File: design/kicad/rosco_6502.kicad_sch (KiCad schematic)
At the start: 58 parts, among them IC1 W65C02SxP, IC2 ATF22V10C-7PX, IC3 XR68C681CJTR-F, IC4 NE555P, IC5 ATF22V10C-7PX, J1 UART_A, J2 UART_B, J3 Conn_01x06, J4 Conn_01x01_Male, J5 Conn_02x18_Odd_Even, J6 Conn_01x02_Pin, J7 Jack-DC, Q1 3.6864MHz, U1 AS6C4008-55PCN, U2 AS6C62256-55PCN, U3 AT28C256-15PU, U4 74HCT174, X1 14MHz

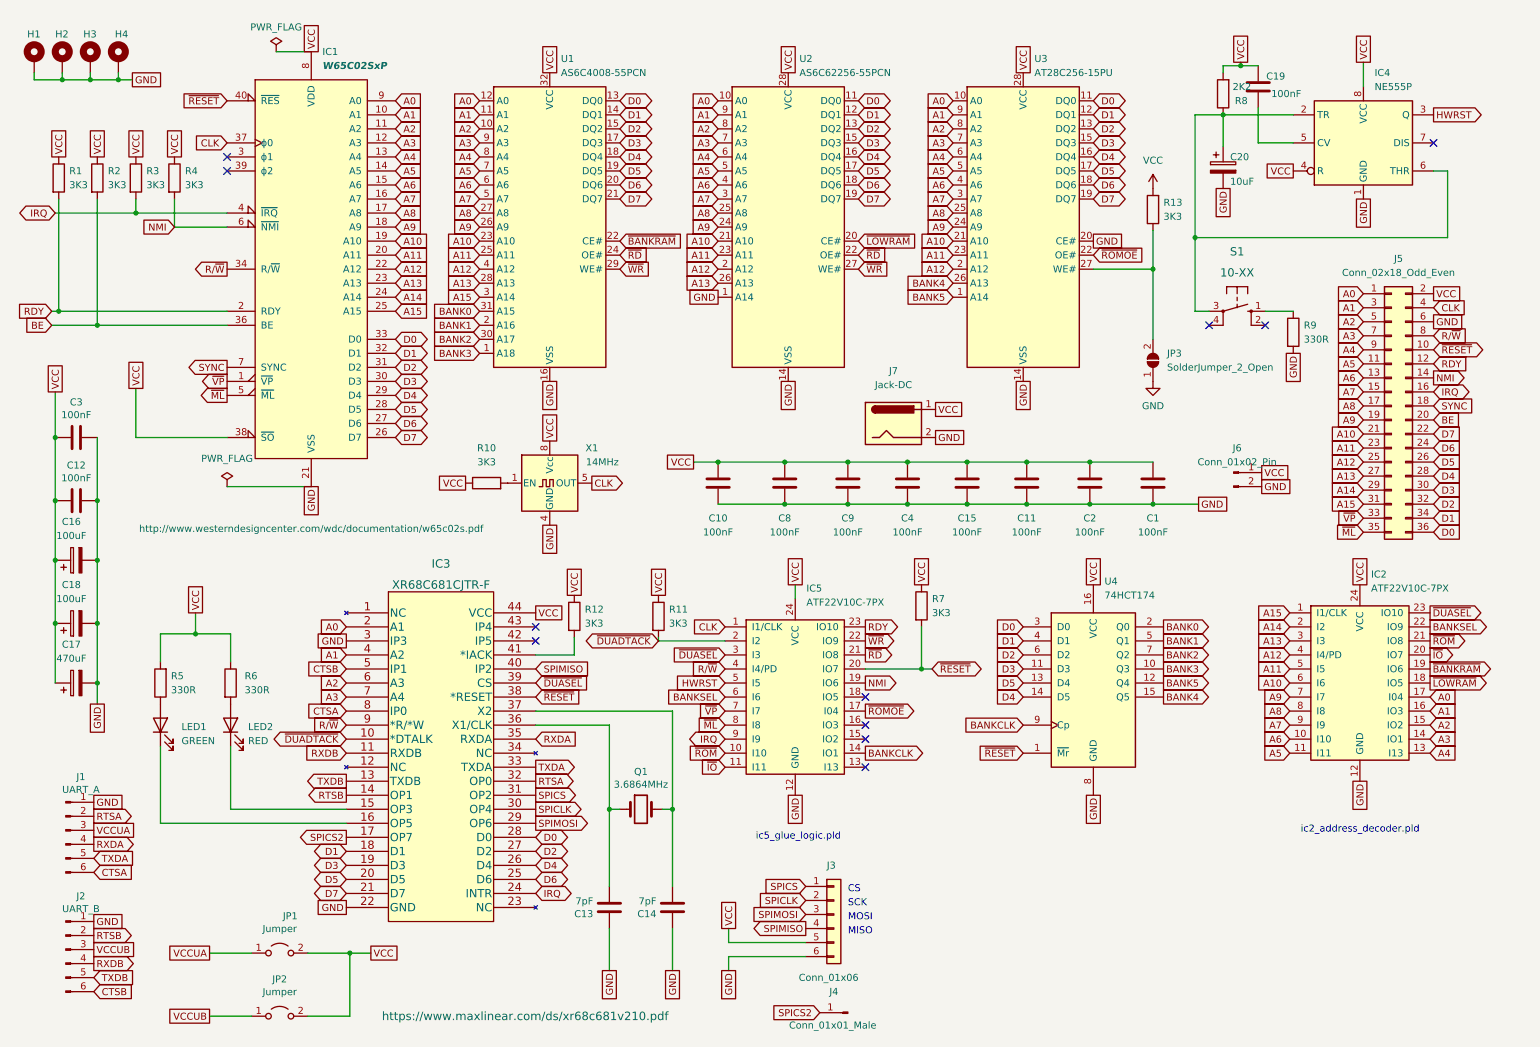
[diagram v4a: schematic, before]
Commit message: Switch ROM to SST39SF010
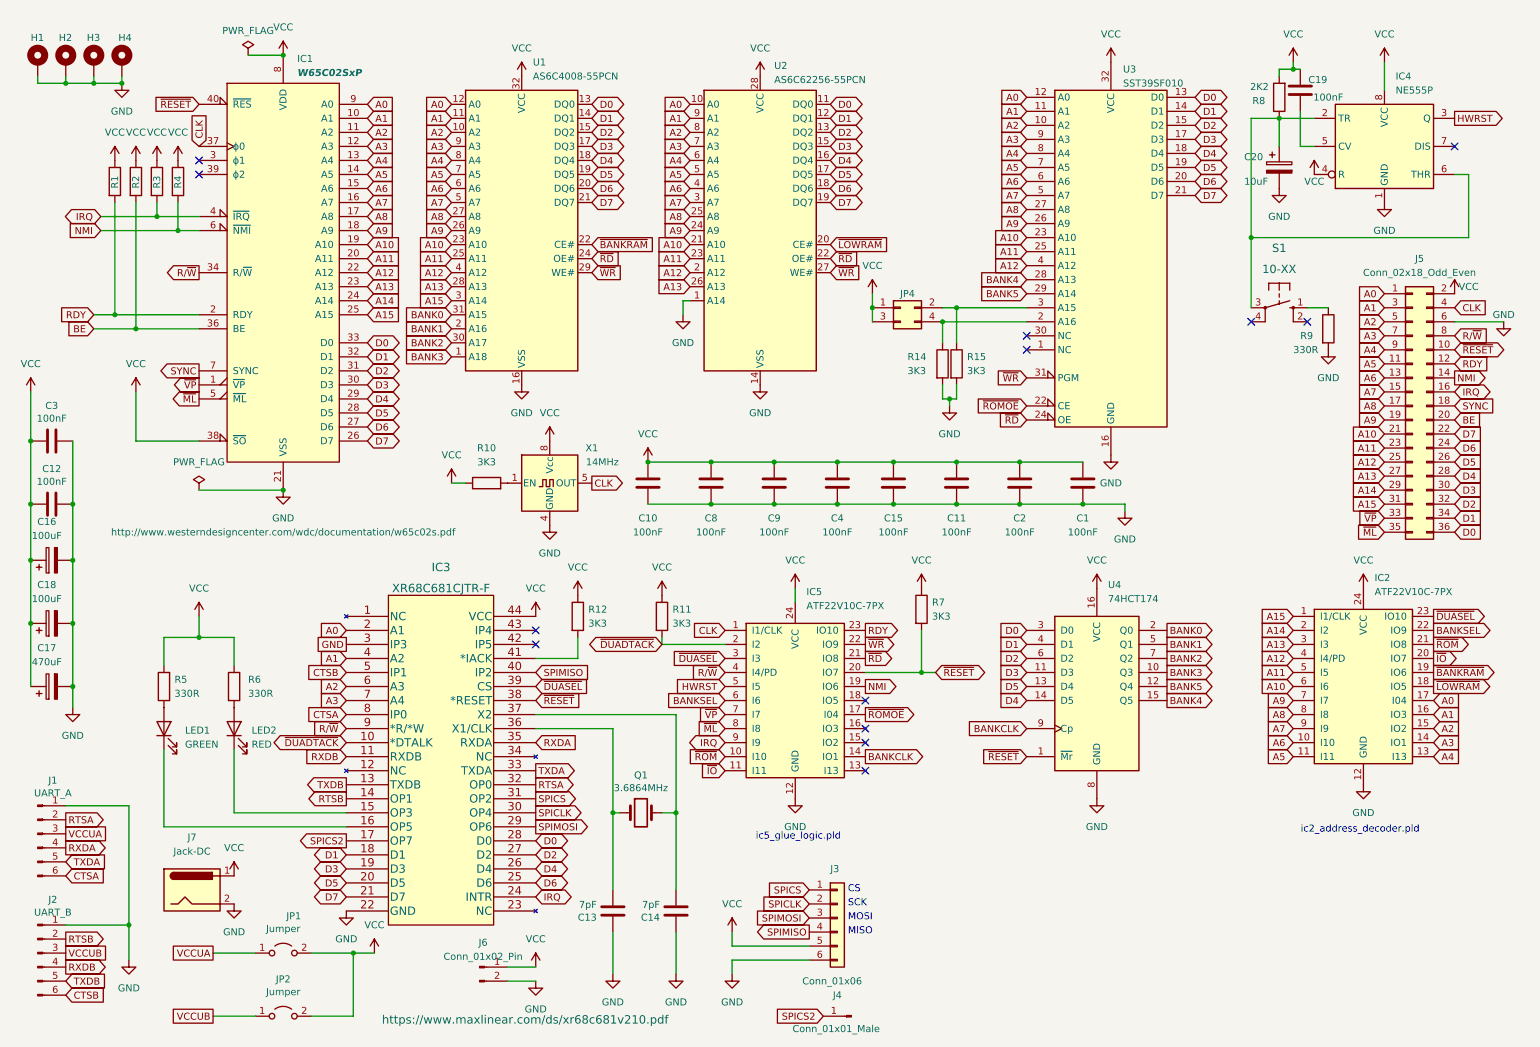
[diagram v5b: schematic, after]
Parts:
- removed JP3: SolderJumper_2_Open, Jumper:SolderJumper-2_P1.3mm_Open_TrianglePad1.0x1.5mm, symbol Jumper:SolderJumper_2_Open
- removed R13: 3K3, Resistor_THT:R_Axial_DIN0207_L6.3mm_D2.5mm_P10.16mm_Horizontal, symbol Device:R
- removed U3: AT28C256-15PU, Package_DIP:DIP-28_W15.24mm_Socket_LongPads, symbol rosco_6502:AT28C256
- added JP4: Conn_02x02_Odd_Even, Connector_PinHeader_2.54mm:PinHeader_2x02_P2.54mm_Vertical, symbol Connector_Generic:Conn_02x02_Odd_Even
- added R14, R15: 3K3, Resistor_THT:R_Axial_DIN0207_L6.3mm_D2.5mm_P10.16mm_Horizontal, symbol Device:R
- added U3: SST39SF010, Package_DIP:DIP-32_W15.24mm_Socket_LongPads, symbol Memory_Flash:SST39SF010
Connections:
- net A0: now also U3.12 (A0)
- net A1: now also U3.11 (A1)
- net A10: now also U3.23 (A10)
- net A11: now also U3.25 (A11)
- net A12: now also U3.4 (A12)
- net A2: now also U3.10 (A2)
- net A3: now also U3.9 (A3)
- net A4: now also U3.8 (A4)
- net A5: now also U3.7 (A5)
- net A6: now also U3.6 (A6)
- net A7: now also U3.5 (A7)
- net A8: now also U3.27 (A8)
- net A9: now also U3.26 (A9)
- net BANK4: now also U3.28 (A13)
- net BANK5: now also U3.29 (A14)
- net D0: now also U3.13 (D0)
- net D1: now also U3.14 (D1)
- net D2: now also U3.15 (D2)
- net D3: now also U3.17 (D3)
- net D4: now also U3.18 (D4)
- net D5: now also U3.19 (D5)
- net D6: now also U3.20 (D6)
- net D7: now also U3.21 (D7)
- net GND: now also R14.2, R15.2, U3.16 (GND)
- net VCC: now also JP4.1 (Pin_1), JP4.3 (Pin_3), U3.32 (VCC)
- net ~{RD}: now also U3.24 (OE)
- net ~{ROMOE}: now also U3.22 (CE)
- net ~{WR}: now also U3.31 (PGM)
- new net: JP4.4 (Pin_4), R14.1, U3.2 (A16)
- new net: JP4.2 (Pin_2), R15.1, U3.3 (A15)
- no-connect marks 11 -> 13
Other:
- moved on the sheet: C1, C10, C11, C12, C13, C14, C15, C16, C17, C18, C19, C2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

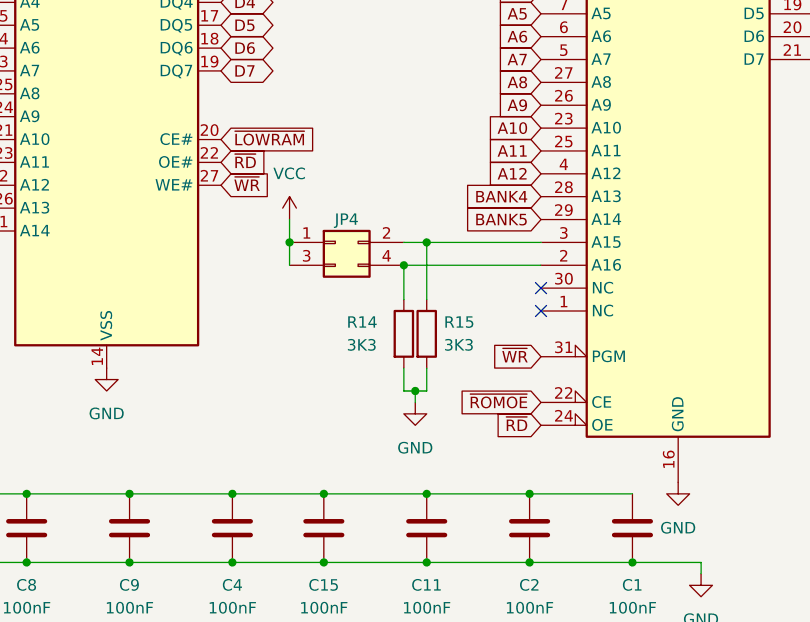
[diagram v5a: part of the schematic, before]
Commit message: Update for larger ROM mapping
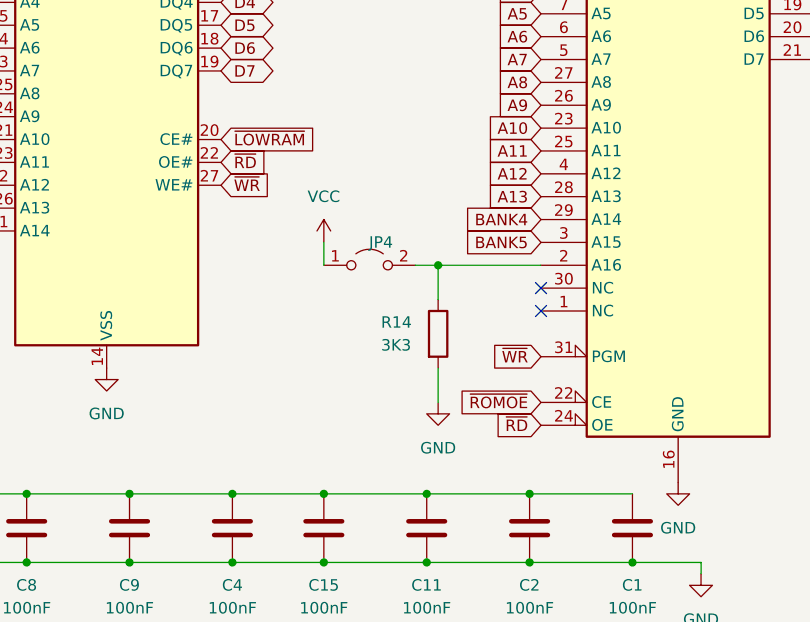
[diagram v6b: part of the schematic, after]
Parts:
- removed R15: 3K3, Resistor_THT:R_Axial_DIN0207_L6.3mm_D2.5mm_P10.16mm_Horizontal, symbol Device:R
- JP4: footprint Connector_PinHeader_2.54mm:PinHeader_2x02_P2.54mm_Vertical -> Connector_PinHeader_2.54mm:PinHeader_1x02_P2.54mm_Vertical; symbol Connector_Generic:Conn_02x02_Odd_Even -> Jumper:Jumper_2_Open
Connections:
- net A13: now also U3.28 (A13)
- net BANK4: now also U3.29 (A14); no longer U3.28 (A13)
- net BANK5: now also U3.3 (A15); no longer U3.29 (A14)
- net VCC: no longer JP4.3 (Pin_3)
- net at R14.1, U3.2 (A16): now also JP4.2 (B); no longer JP4.4 (Pin_4)
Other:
- moved on the sheet: R14
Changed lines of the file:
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@@
   (junction (at 149.86 100.33) (diameter 0) (color 0 0 0 0)
   )
+  (junction (at 184.15 67.31) (diameter 0) (color 0 0 0 0)
+  )
   (junction (at 171.45 100.33) (diameter 0) (color 0 0 0 0)
   )
@@
   (junction (at 132.08 156.21) (diameter 0) (color 0 0 0 0)
   )
-  (junction (at 182.88 64.77) (diameter 0) (color 0 0 0 0)
-  )
   (junction (at 161.29 100.33) (diameter 0) (color 0 0 0 0)
   )
@@
   (junction (at 194.31 100.33) (diameter 0) (color 0 0 0 0)
   )
-  (junction (at 180.34 67.31) (diameter 0) (color 0 0 0 0)
-  )
-  (junction (at 167.64 64.77) (diameter 0) (color 0 0 0 0)
-  )
   (junction (at 34.29 68.58) (diameter 0) (color 0 0 0 0)
   )
-  (junction (at 181.61 81.28) (diameter 0) (color 0 0 0 0)
-  )
   (junction (at 45.72 124.46) (diameter 0) (color 0 0 0 0)
   )
@@
     (stroke (width 0) (type default))
   )
-  (wire (pts (xy 181.61 81.28) (xy 181.61 82.55))
-    (stroke (width 0) (type default))
-  )
   (wire (pts (xy 91.44 96.52) (xy 93.98 96.52))
     (stroke (width 0) (type default))
@@
     (stroke (width 0) (type default))
   )
-  (wire (pts (xy 180.34 64.77) (xy 182.88 64.77))
-    (stroke (width 0) (type default))
-  )
   (wire (pts (xy 132.08 156.21) (xy 132.08 170.18))
     (stroke (width 0) (type default))
@@
     (stroke (width 0) (type default))
   )
-  (wire (pts (xy 180.34 78.74) (xy 180.34 81.28))
-    (stroke (width 0) (type default))
-  )
-  (wire (pts (xy 182.88 78.74) (xy 182.88 81.28))
+  (wire (pts (xy 184.15 78.74) (xy 184.15 82.55))
     (stroke (width 0) (type default))
   )
@@
     (stroke (width 0) (type default))
   )
-  (wire (pts (xy 181.61 81.28) (xy 182.88 81.28))
-    (stroke (width 0) (type default))
-  )
   (wire (pts (xy 30.48 45.72) (xy 30.48 66.04))
     (stroke (width 0) (type default))
@@
     (stroke (width 0) (type default))
   )
-  (wire (pts (xy 167.64 62.23) (xy 167.64 64.77))
+  (wire (pts (xy 171.45 64.77) (xy 171.45 67.31))
     (stroke (width 0) (type default))
   )
@@
     (stroke (width 0) (type default))
   )
-  (wire (pts (xy 180.34 67.31) (xy 180.34 71.12))
+  (wire (pts (xy 184.15 67.31) (xy 184.15 71.12))
     (stroke (width 0) (type default))
   )
@@
     (stroke (width 0) (type default))
   )
-  (wire (pts (xy 180.34 67.31) (xy 195.58 67.31))
-    (stroke (width 0) (type default))
-  )
   (wire (pts (xy 26.67 66.04) (xy 30.48 66.04))
     (stroke (width 0) (type default))
@@
     (stroke (width 0) (type default))
   )
-  (wire (pts (xy 167.64 64.77) (xy 167.64 67.31))
-    (stroke (width 0) (type default))
-  )
   (wire (pts (xy 72.39 158.75) (xy 39.37 158.75))
     (stroke (width 0) (type default))
@@
     (stroke (width 0) (type default))
   )
-  (wire (pts (xy 182.88 71.12) (xy 182.88 64.77))
-    (stroke (width 0) (type default))
-  )
   (wire (pts (xy 161.29 92.71) (xy 149.86 92.71))
     (stroke (width 0) (type default))
@@
     (stroke (width 0) (type default))
   )
+  (wire (pts (xy 184.15 67.31) (xy 195.58 67.31))
+    (stroke (width 0) (type default))
+  )
   (wire (pts (xy 132.08 138.43) (xy 132.08 156.21))
     (stroke (width 0) (type default))
@@
     (stroke (width 0) (type default))
   )
-  (wire (pts (xy 180.34 81.28) (xy 181.61 81.28))
-    (stroke (width 0) (type default))
-  )
   (wire (pts (xy 34.29 88.9) (xy 34.29 80.01))
     (stroke (width 0) (type default))
@@
     (stroke (width 0) (type default))
   )
+  (wire (pts (xy 181.61 67.31) (xy 184.15 67.31))
+    (stroke (width 0) (type default))
+  )
   (wire (pts (xy 114.3 128.27) (xy 106.68 128.27))
     (stroke (width 0) (type default))
@@
     (stroke (width 0) (type default))
   )
-  (wire (pts (xy 182.88 64.77) (xy 195.58 64.77))
-    (stroke (width 0) (type default))
-  )
   (text "ic5_glue_logic.pld" (at 161.925 161.29 0)
     (effects (font (size 1.27 1.27)) (justify right bottom))
@@
     )
   )
-  (global_label "BANK5" (shape input) (at 195.58 62.23 180) (fields_autoplaced)
+  (global_label "BANK5" (shape input) (at 195.58 64.77 180) (fields_autoplaced)
     (effects (font (size 1.27 1.27)) (justify right))
-    (property "Intersheetrefs" "${INTERSHEET_REFS}" (at 186.9983 62.1506 0)
+    (property "Intersheetrefs" "${INTERSHEET_REFS}" (at 186.9983 64.6906 0)
       (effects (font (size 1.27 1.27)) (justify right) hide)
     )
@@
     )
   )
+  (global_label "A13" (shape input) (at 195.58 59.69 180) (fields_autoplaced)
+    (effects (font (size 1.27 1.27)) (justify right))
+    (property "Intersheetrefs" "${INTERSHEET_REFS}" (at 189.0872 59.69 0)
+      (effects (font (size 1.27 1.27)) (justify right) hide)
+    )
+  )
   (global_label "~{BANKRAM}" (shape input) (at 116.84 53.34 0) (fields_autoplaced)
     (effects (font (size 1.27 1.27)) (justify left))
@@
     )
   )
-  (global_label "BANK4" (shape input) (at 195.58 59.69 180) (fields_autoplaced)
+  (global_label "BANK4" (shape input) (at 195.58 62.23 180) (fields_autoplaced)
     (effects (font (size 1.27 1.27)) (justify right))
-    (property "Intersheetrefs" "${INTERSHEET_REFS}" (at 186.9983 59.6106 0)
+    (property "Intersheetrefs" "${INTERSHEET_REFS}" (at 186.9983 62.1506 0)
       (effects (font (size 1.27 1.27)) (justify right) hide)
     )
@@
     )
   )
-  (symbol (lib_id "Device:R") (at 180.34 74.93 0) (unit 1)
+  (symbol (lib_id "Device:R") (at 184.15 74.93 0) (unit 1)
     (in_bom yes) (on_board yes) (dnp no)
-    (property "Reference" "R14" (at 173.99 73.66 0)
+    (property "Reference" "R14" (at 177.8 73.66 0)
       (effects (font (size 1.27 1.27)) (justify left))
     )
-    (property "Value" "3K3" (at 173.99 76.2 0)
+    (property "Value" "3K3" (at 177.8 76.2 0)
       (effects (font (size 1.27 1.27)) (justify left))
     )
-    (property "Footprint" "Resistor_THT:R_Axial_DIN0207_L6.3mm_D2.5mm_P10.16mm_Horizontal" (at 178.562 74.93 90)
+    (property "Footprint" "Resistor_THT:R_Axial_DIN0207_L6.3mm_D2.5mm_P10.16mm_Horizontal" (at 182.372 74.93 90)
       (effects (font (size 1.27 1.27)) hide)
     )
-    (property "Datasheet" "~" (at 180.34 74.93 0)
+    (property "Datasheet" "~" (at 184.15 74.93 0)
       (effects (font (size 1.27 1.27)) hide)
     )
@@
     )
   )
-  (symbol (lib_id "power:GND") (at 181.61 82.55 0) (unit 1)
+  (symbol (lib_id "power:GND") (at 184.15 82.55 0) (unit 1)
     (in_bom yes) (on_board yes) (dnp no) (fields_autoplaced)
-    (property "Reference" "#PWR051" (at 181.61 88.9 0)
+    (property "Reference" "#PWR051" (at 184.15 88.9 0)
       (effects (font (size 1.27 1.27)) hide)
     )
-    (property "Value" "GND" (at 181.61 87.63 0)
+    (property "Value" "GND" (at 184.15 87.63 0)
       (effects (font (size 1.27 1.27)))
     )
-    (property "Footprint" "" (at 181.61 82.55 0)
+    (property "Footprint" "" (at 184.15 82.55 0)
       (effects (font (size 1.27 1.27)) hide)
     )
-    (property "Datasheet" "" (at 181.61 82.55 0)
+    (property "Datasheet" "" (at 184.15 82.55 0)
       (effects (font (size 1.27 1.27)) hide)
     )
@@
     )
   )
-  (symbol (lib_id "Connector_Generic:Conn_02x02_Odd_Even") (at 172.72 64.77 0) (unit 1)
+  (symbol (lib_id "Jumper:Jumper_2_Open") (at 176.53 67.31 0) (unit 1)
     (in_bom yes) (on_board yes) (dnp no)
-    (property "Reference" "JP4" (at 173.99 62.23 0)
+    (property "Reference" "JP4" (at 177.8 64.77 0)
       (effects (font (size 1.27 1.27)))
     )
-    (property "Value" "Conn_02x02_Odd_Even" (at 173.99 60.96 0)
+    (property "Value" "Conn_02x02_Odd_Even" (at 177.8 63.5 0)
       (effects (font (size 1.27 1.27)) hide)
     )
-    (property "Footprint" "Connector_PinHeader_2.54mm:PinHeader_2x02_P2.54mm_Vertical" (at 172.72 64.77 0)
+    (property "Footprint" "Connector_PinHeader_2.54mm:PinHeader_1x02_P2.54mm_Vertical" (at 176.53 67.31 0)
       (effects (font (size 1.27 1.27)) hide)
     )
-    (property "Datasheet" "~" (at 172.72 64.77 0)
+    (property "Datasheet" "~" (at 176.53 67.31 0)
       (effects (font (size 1.27 1.27)) hide)
     )
     (pin "2")
     (pin "1")
-    (pin "4")
-    (pin "3")
     (instances
       (project "rosco_6502"
@@
     )
   )
-  (symbol (lib_id "power:VCC") (at 167.64 62.23 0) (unit 1)
+  (symbol (lib_id "power:VCC") (at 171.45 64.77 0) (unit 1)
     (in_bom yes) (on_board yes) (dnp no) (fields_autoplaced)
-    (property "Reference" "#PWR028" (at 167.64 66.04 0)
+    (property "Reference" "#PWR028" (at 171.45 68.58 0)
       (effects (font (size 1.27 1.27)) hide)
     )
-    (property "Value" "VCC" (at 167.64 57.15 0)
+    (property "Value" "VCC" (at 171.45 59.69 0)
       (effects (font (size 1.27 1.27)))
     )
-    (property "Footprint" "" (at 167.64 62.23 0)
+    (property "Footprint" "" (at 171.45 64.77 0)
       (effects (font (size 1.27 1.27)) hide)
     )
-    (property "Datasheet" "" (at 167.64 62.23 0)
+    (property "Datasheet" "" (at 171.45 64.77 0)
       (effects (font (size 1.27 1.27)) hide)
     )
@@
         )
       )
-    )
-  )
-  (symbol (lib_id "Device:R") (at 182.88 74.93 0) (unit 1)
-    (in_bom yes) (on_board yes) (dnp no)
-    (property "Reference" "R15" (at 184.785 73.6599 0)
-      (effects (font (size 1.27 1.27)) (justify left))
-    )
-    (property "Value" "3K3" (at 184.785 76.1999 0)
-      (effects (font (size 1.27 1.27)) (justify left))
-    )
-    (property "Footprint" "Resistor_THT:R_Axial_DIN0207_L6.3mm_D2.5mm_P10.16mm_Horizontal" (at 181.102 74.93 90)
-      (effects (font (size 1.27 1.27)) hide)
-    )
-    (property "Datasheet" "~" (at 182.88 74.93 0)
-      (effects (font (size 1.27 1.27)) hide)
-    )
-    (pin "1")
-    (pin "2")
-    (instances
-      (project "rosco_6502"
-        (path "/e63e39d7-6ac0-4ffd-8aa3-1841a4541b55"
-          (reference "R15") (unit 1)
-        )
-      )
